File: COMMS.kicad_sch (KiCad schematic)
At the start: 44 parts, among them J11 1840461-1, U6 KSZ9031RNXIA, U7 25MHz

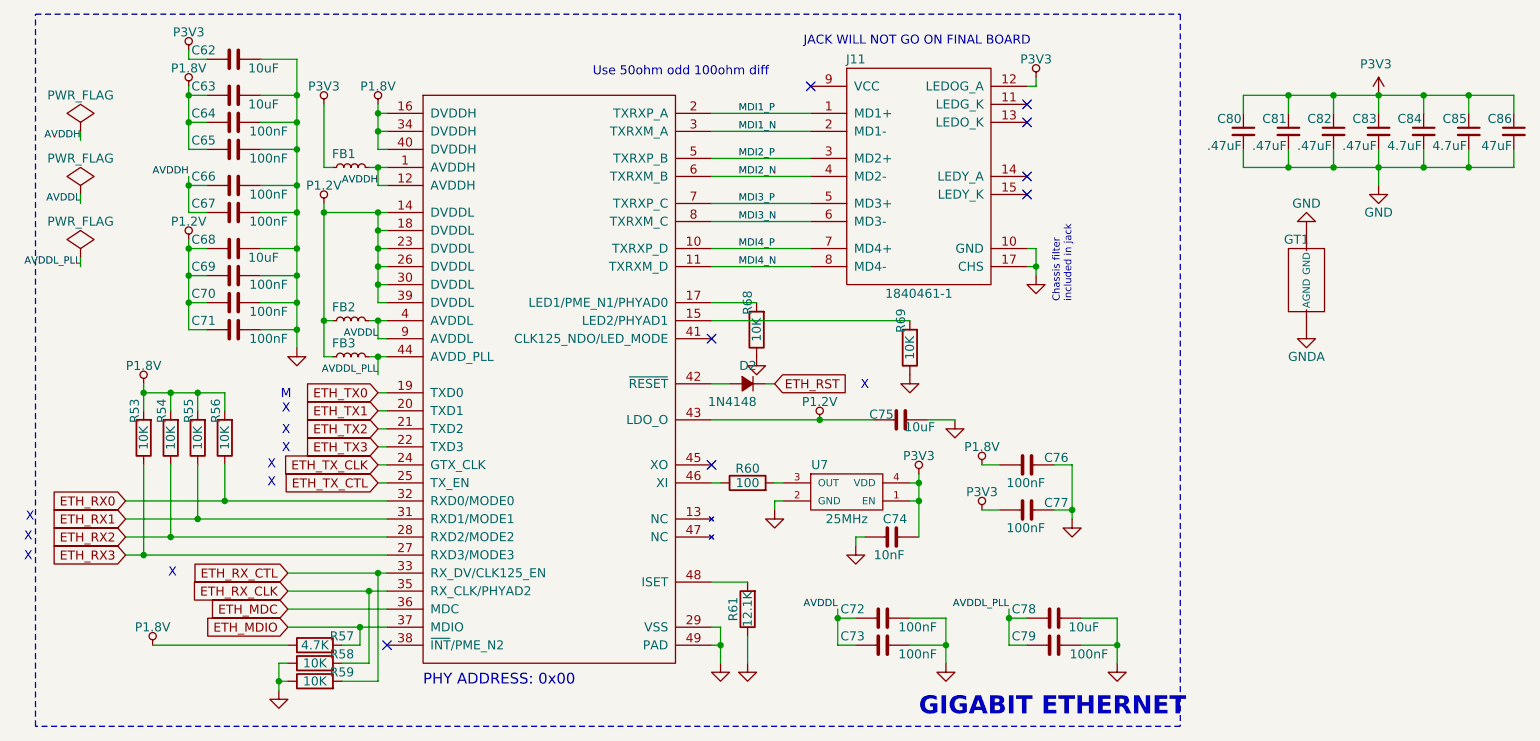
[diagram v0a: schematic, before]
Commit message: updated layouts, added motor
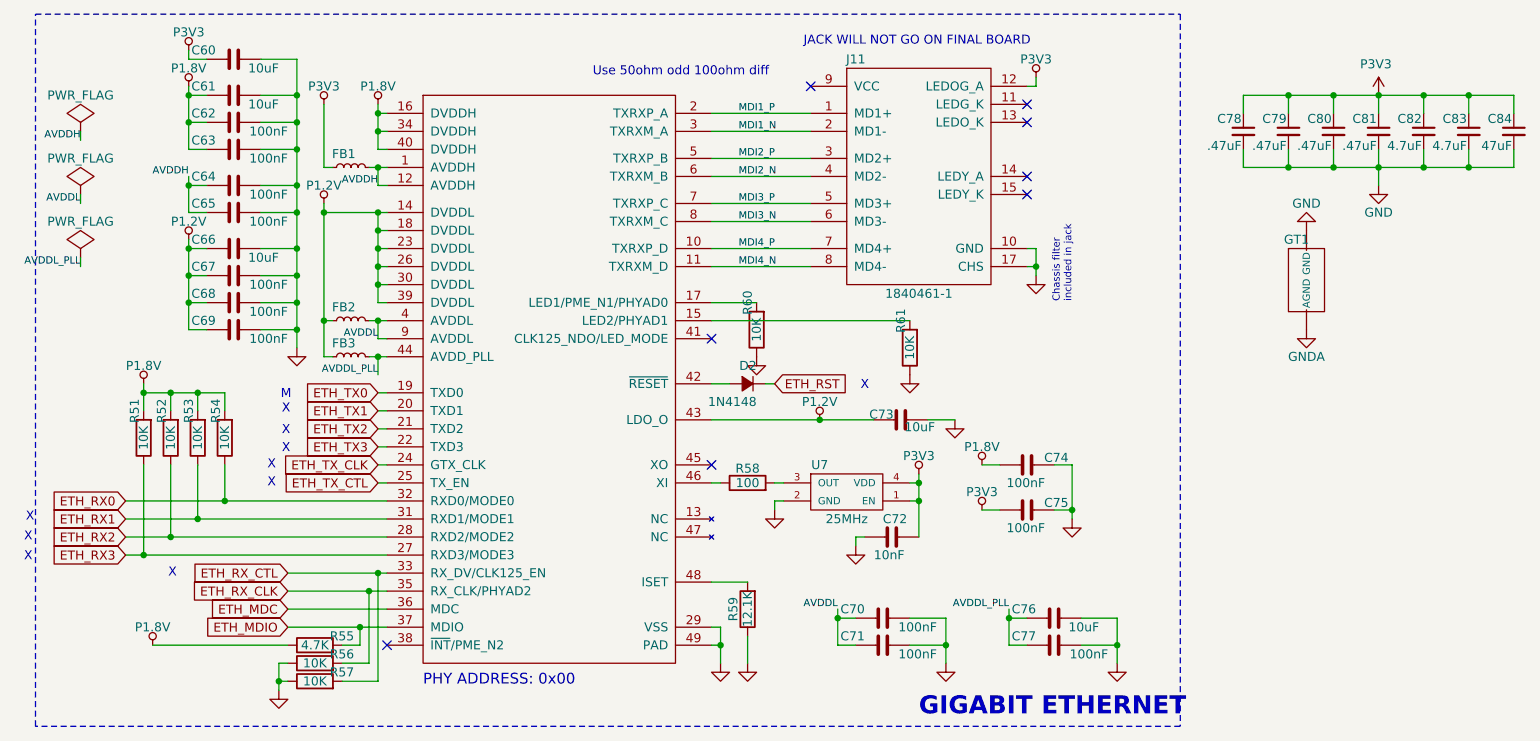
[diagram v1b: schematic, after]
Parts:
- renumbered C62 to C60, C63 to C61, C64 to C62, C65 to C63, C66 to C64, C67 to C65, C68 to C66, C69 to C67, C70 to C68, C71 to C69, C72 to C70, C73 to C71, C74 to C72, C75 to C73, C76 to C74, C77 to C75, C78 to C76, C79 to C77, C80 to C78, C81 to C79, C82 to C80, C83 to C81, C84 to C82, C85 to C83, C86 to C84, R53 to R51, R54 to R52, R55 to R53, R56 to R54, R57 to R55, R58 to R56, R59 to R57, R60 to R58, R61 to R59, R68 to R60, R69 to R61

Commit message: Changes to layout pins
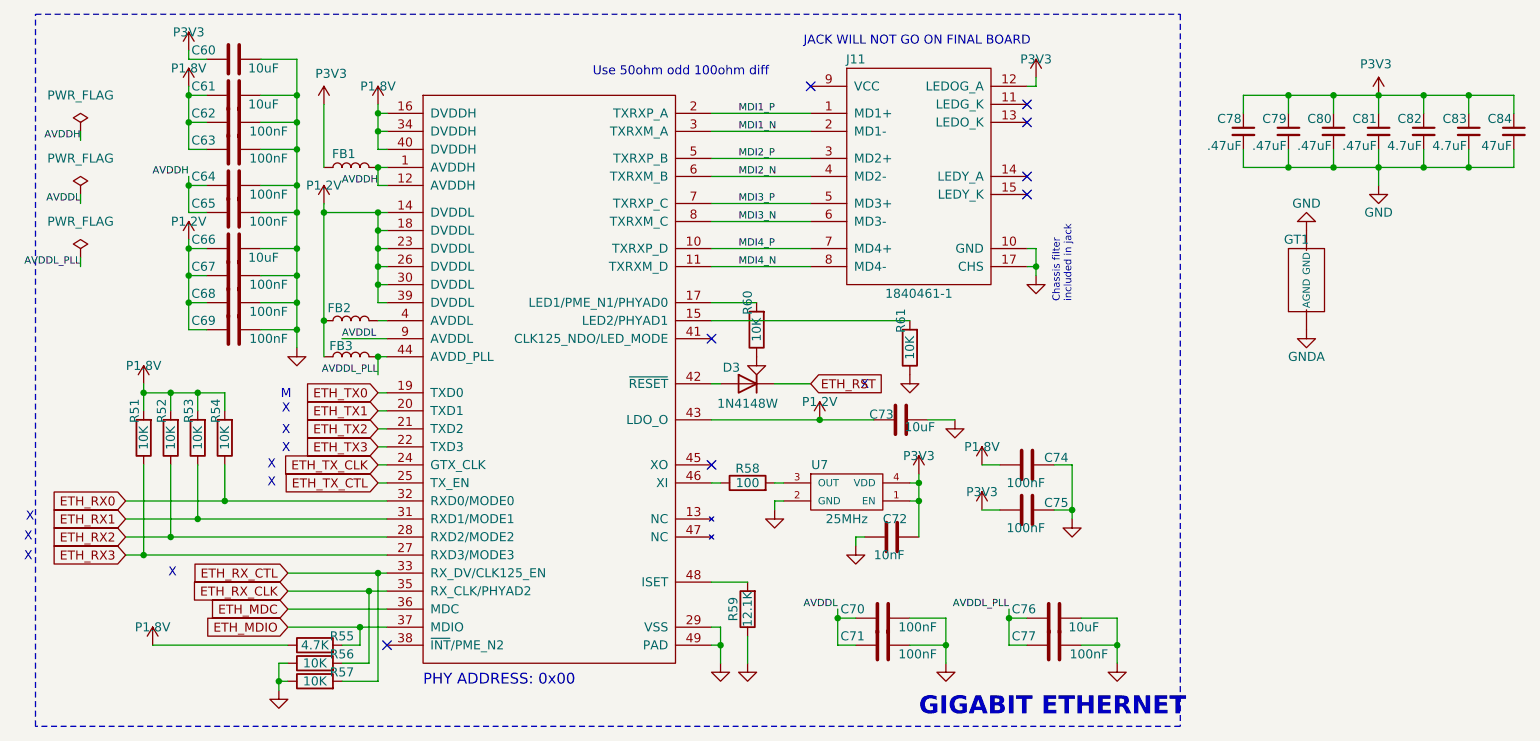
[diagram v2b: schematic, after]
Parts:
- removed D2: 1N4148, to-sod-sot:SOD-323, symbol CIAA_ACC:D
- added D3: 1N4148W, Diode_THT:D_DO-35_SOD27_P3.81mm_Vertical_CathodeUp, symbol Diode:1N4148W
- C60, C61, C62, C63, C64, C65, C66, C67, C68, C69, C70, C71, C72, C73, C74, C75, C76, C77: symbol CIAA_ACC:C -> Device:C
- FB1, FB2, FB3: symbol CIAA_ACC:L -> Device:L
- R51, R52, R53, R54, R55, R56, R57, R58, R59, R60, R61: symbol CIAA_ACC:R -> Device:R
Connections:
- net AVDDL: no longer FB2.2, U6.4 (AVDDL)
- net ETH_RST: now also D3.1 (K)
- net at U6.42 (~{RESET}): now also D3.2 (A)
- new net: FB2.2, U6.4 (AVDDL)
